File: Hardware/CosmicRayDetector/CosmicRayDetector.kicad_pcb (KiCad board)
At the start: 2 copper layers, 40 x 70 mm, 80 parts, among them J1 Conn_01x04, J2 Conn_02x06_Odd_Even, J3 Conn_01x01_Female, J4 Conn_01x01_Female, J5 Conn_01x01_Female, J6 Conn_01x01_Female, J7 Conn_01x01_Female, J8 USB_B_Micro, Q1 BC848, Q2 BC848, Q3 BC848, Q4 BC859, Q5 BC859, Q6 BC859, Q7 BC848, Q8 BC859, SW1 SW_Push, SW2 SW_Push, U1 HEF4093B, U2 AZ1117-3.3

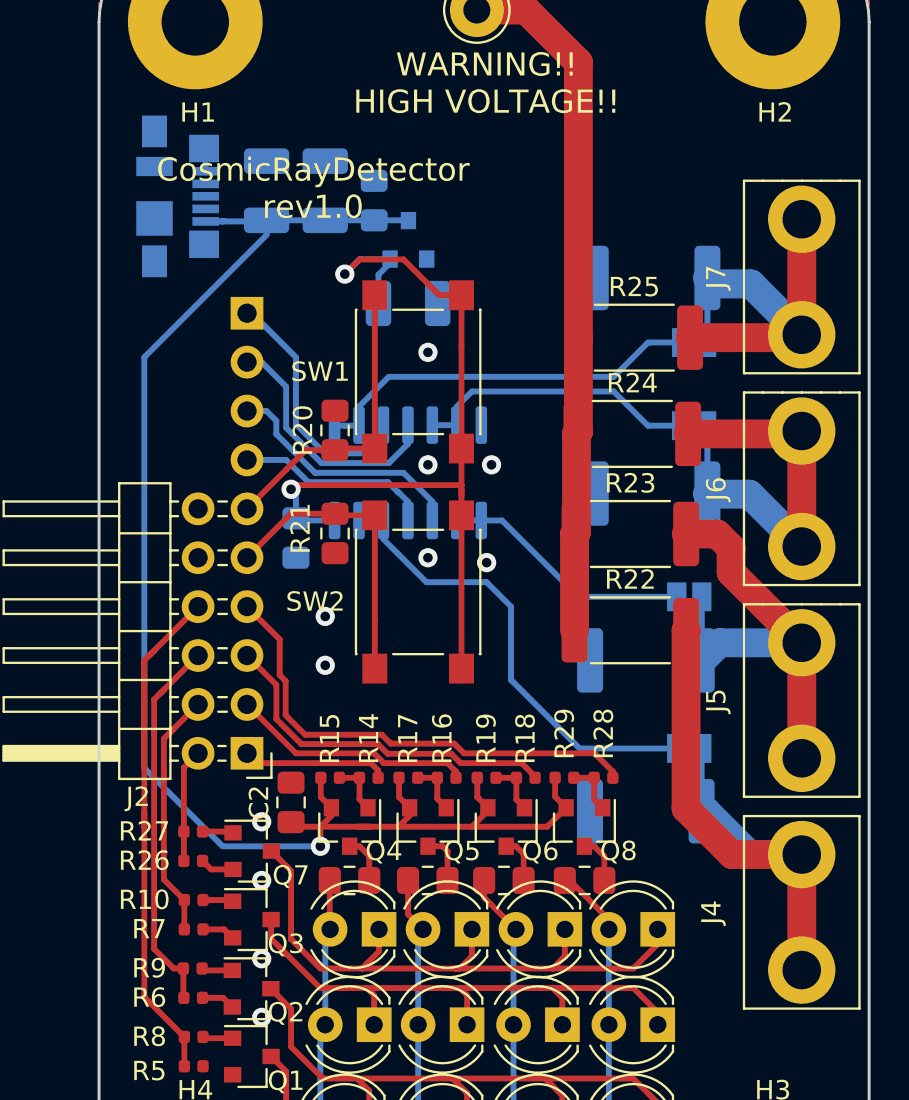
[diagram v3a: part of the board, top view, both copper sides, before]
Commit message: add bom
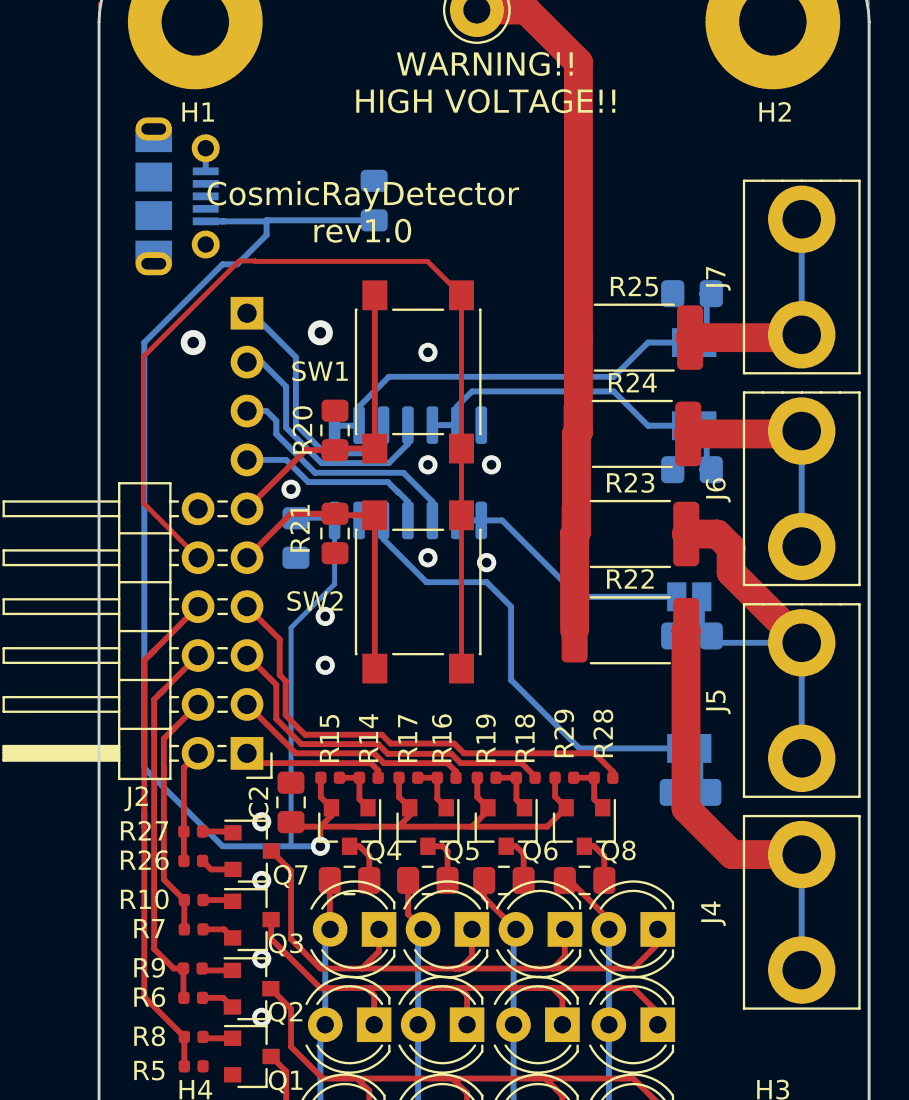
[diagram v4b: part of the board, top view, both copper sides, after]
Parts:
- removed C7, C8, C9: 10u, Capacitor_Tantalum_SMD:CP_EIA-3528-21_Kemet-B
- removed U2: AZ1117-3.3, Package_TO_SOT_SMD:SOT-23
- J8: footprint Connector_USB:USB_Micro-B_Molex_47346-0001 -> Connector_USB:USB_Micro-B_Molex-105017-0001
- R1, R2, R3, R4: footprint Resistor_SMD:R_2512_6332Metric -> Resistor_SMD:R_0805_2012Metric_Pad1.20x1.40mm_HandSolder
- R11, R12, R13, R30: value 10k -> 1k
- moved R2 2.71 mm to (50.8, 56.9)
- moved R1 2.52 mm to (50.7, 65.0)
- moved R3 2.44 mm to (50.8, 48.3)
- moved R4 2.25 mm to (50.8, 39.1)
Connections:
- C5 pad 1: +3V3 -> +5V
- J2 pad 10: GND -> /UserInterface/BUTTON_VCC
- SW1 pad 2: +3V3 -> /UserInterface/BUTTON_VCC
- SW2 pad 2: +3V3 -> /UserInterface/BUTTON_VCC
- U1 pad 14: +3V3 -> +5V
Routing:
- net /UserInterface/BUTTON_VCC: track 0.00 -> 50.3 mm
- net +3V3: track 46.3 -> 0.67 mm, vias 2 -> 1
- net +5V: track 80.0 -> 98.6 mm
- net GM_CONNECTOR_3: track 21.6 -> 19.5 mm
- net GM_CONNECTOR_4: track 21.4 -> 19.6 mm
- net GM_CONNECTOR_2: track 24.3 -> 22.8 mm
- net Net-(J1-Pad2): vias 1 -> 0
- net GND: vias 15 -> 17
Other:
- net class high voltage: clearance 2.75 -> 0.1778

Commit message: fix #103 #104 #105 #106
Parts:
- R22, R23, R24, R25: value 6M8 -> 5M1; footprint Resistor_SMD:R_2512_6332Metric -> Resistor_THT:R_Axial_DIN0411_L9.9mm_D3.6mm_P12.70mm_Horizontal
- moved R25 15.7 mm to (43.2, 26.4), turned to 315 degrees
- moved R24 13.0 mm to (42.9, 34.3), turned to 315 degrees
- moved R23 9.96 mm to (43.2, 42.7), turned to 315 degrees
- moved C6 5.87 mm to (28.7, 36.1), turned to 0 degrees
- moved R22 5.49 mm to (43.2, 53.3), turned to 315 degrees
- moved JP2 2.29 mm to (50.8, 65.0)
- moved R1 2.03 mm to (50.8, 67.1)
- moved JP1 1.52 mm to (50.9, 40.1)
- moved R4 1.02 mm to (50.8, 38.1)
- moved JP4 0.76 mm to (50.9, 46.7)
- moved R3 0.51 mm to (50.8, 48.8)
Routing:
- net Net-(JP4-Pad2): track 15.0 -> 26.2 mm
- net GM_CONNECTOR_1: track 32.0 -> 23.0 mm
- net +5V: track 98.6 -> 91.0 mm
- net Net-(JP1-Pad2): track 20.4 -> 26.1 mm
- net /HVConnector/HIGH_VOLTAGE: track 36.2 -> 31.8 mm
- net GM_CONNECTOR_4: track 19.6 -> 18.4 mm
- net Net-(JP2-Pad2): track 24.2 -> 23.1 mm
- net Net-(JP3-Pad2): track 13.1 -> 14.0 mm
- net GND: vias 17 -> 14

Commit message: fix #109, fix #110
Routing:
- net /UserInterface/BUTTON_VCC: track 50.3 -> 51.6 mm
- net GM_CONNECTOR_2: track 23.1 -> 21.9 mm
- net GM_CONNECTOR_3: track 19.4 -> 20.3 mm
- net GM_CONNECTOR_1: track 23.0 -> 22.1 mm
- net /UserInterface/LED_X_1: track 27.3 -> 28.0 mm
- net +3V3: track 0.67 -> 0.00 mm, vias 1 -> 0
- net Net-(JP3-Pad2): track 14.0 -> 14.6 mm
- net Net-(J1-Pad1): track 13.3 -> 13.9 mm
- net /UserInterface/LED_X_3: track 13.7 -> 14.3 mm
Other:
- board text added: "1"
- board text added: "BUTT"
- board text added: "BUTTON_1"
- board text added: "BUTTON_2"
- board text added: "GM1"
- board text added: "GM2"
- board text added: "GM3"
- board text added: "GM4"
- board text added: "GND"
- board text added: "LED"
- board text added: "Vcc"
- board text added: "X_1"
- board text added: "X_2"
- board text added: "X_3"
- board text added: "X_4"
- board text added: "Y_1"
- board text added: "Y_2"
- board text added: "Y_3"
- board text added: "Y_4"

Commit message: cleanup after transition to KiCad6
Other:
- net class Default removed
- net class high voltage removed
